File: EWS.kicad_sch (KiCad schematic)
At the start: 4 parts

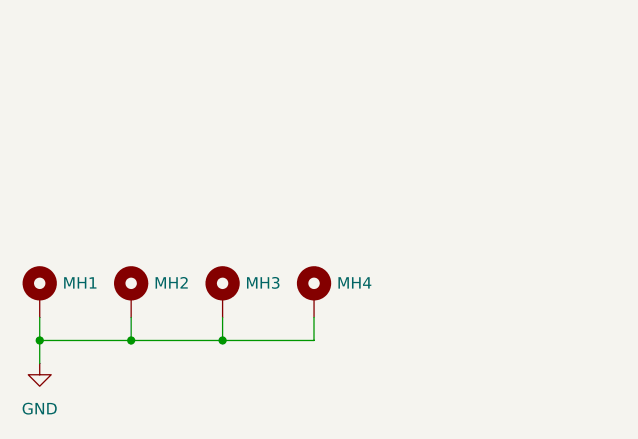
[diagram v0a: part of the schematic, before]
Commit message: Major hardware update: toolhead switching, DC/DC protection, and documentation overhaul
Hardware Changes:
- Replaced reverse polarity protection with 2x PFET toolhead switching (PB2/PA5 control)
- Added SS56 Schottky diode reverse polarity protection for DC/DC converter
- Updated current limit resistor to 5.1kΩ (~10.2A)
- Removed fan control circuitry and JST-XH connector
- Removed internal JST-XH USB port with fuse/protection

Documentation Updates:
- Updated both README files to reflect hardware changes
- Removed all fan control references and configurations
- Updated Klipper configuration examples
- Cleaned up pinout and connector assignments
- Updated technical specifications table
- Fixed table of contents and cross-references
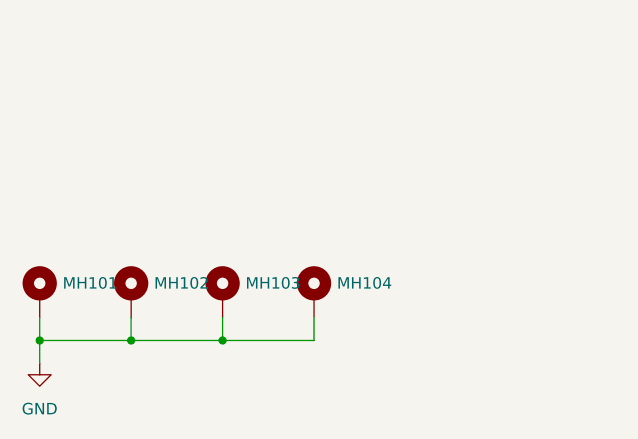
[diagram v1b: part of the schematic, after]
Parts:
- renumbered MH1 to MH101, MH2 to MH102, MH3 to MH103, MH4 to MH104
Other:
- company: (none) -> Eduard Iten
- title: (none) -> EWS - Power, CANbus and USB HAT for 3D Printers
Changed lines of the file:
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@@
 	(generator_version "9.0")
 	(paper "A4")
+	(title_block
+		(title "EWS - Power, CANbus and USB HAT for 3D Printers")
+		(date "2025-12-03")
+		(rev "1.0")
+		(company "Eduard Iten")
+	)
 	(junction
 		(at 54.61 176.53)
@@
 		(on_board yes)
 		(dnp no)
-		(property "Reference" "MH2"
+		(property "Reference" "MH102"
 			(at 46.99 170.18 0)
 			(effects
@@
 			(project "EWS"
 				(path "/4ae99543-64c8-472f-befd-04c32f138656"
-					(reference "MH2")
+					(reference "MH102")
 					(unit 1)
 				)
@@
 		(on_board yes)
 		(dnp no)
-		(property "Reference" "MH3"
+		(property "Reference" "MH103"
 			(at 57.15 170.18 0)
 			(effects
@@
 			(project "EWS"
 				(path "/4ae99543-64c8-472f-befd-04c32f138656"
-					(reference "MH3")
+					(reference "MH103")
 					(unit 1)
 				)
@@
 		(on_board yes)
 		(dnp no)
-		(property "Reference" "MH1"
+		(property "Reference" "MH101"
 			(at 36.83 170.18 0)
 			(effects
@@
 			(project ""
 				(path "/4ae99543-64c8-472f-befd-04c32f138656"
-					(reference "MH1")
+					(reference "MH101")
 					(unit 1)
 				)
@@
 		(on_board yes)
 		(dnp no)
-		(property "Reference" "MH4"
+		(property "Reference" "MH104"
 			(at 67.31 170.18 0)
 			(effects
@@
 			(project "EWS"
 				(path "/4ae99543-64c8-472f-befd-04c32f138656"
-					(reference "MH4")
+					(reference "MH104")
 					(unit 1)
 				)

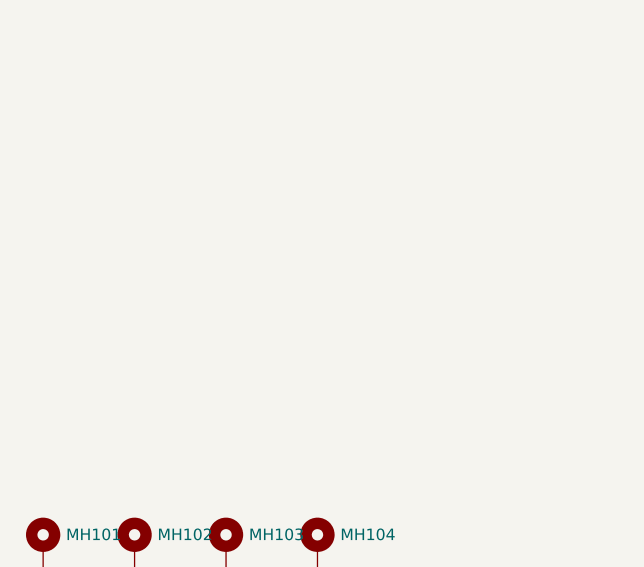
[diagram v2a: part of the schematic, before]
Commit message: Rev 0.2: Major hardware improvements and production readiness
Hardware Improvements (Thanks to shx for schematic cleanup):
- Clean up schematic organization and structure
- Set CAN transceiver Silent pin to GND for stability
- Add status LEDs (yellow: 24V/5V/3.3V, green: MCU PB4)
- Replace jumpers with solder jumpers on bottom side
- Add jumpers to output PFETs for permanent-on without firmware
- Add robust test points for 5V/GND load testing
- Add optional heatsink for DC/DC converter on bottom
- Add 10µF capacitor for MCU on 3.3V rail

Component Optimizations:
- Replace 30kΩ with 33kΩ basic part for simplified BOM
- Change DC/DC feedback: 15.5kΩ15kΩ (new output: 5.1V)
- Upgrade CAN ESD protection: NUP2105LPESD1CAN
- Increase CAN termination resistor footprint: 04020603
- Switch USB hub supply from 5V to 3.3V per datasheet

Production Ready:
- Add all LCSC part numbers and rotations
- Generate complete production data package
- Improve PCB layout and button placement
- Create comprehensive changelog documentation
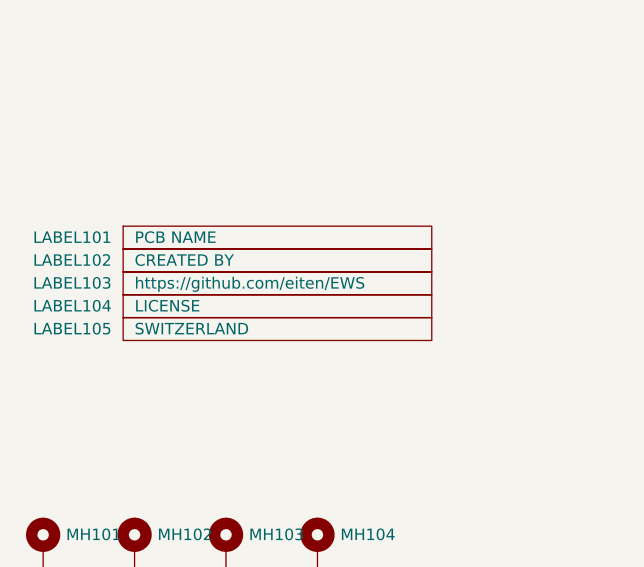
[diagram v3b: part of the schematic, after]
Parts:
- added LABEL101: PCB NAME, project:EWS Rev. 1.0, symbol project:LABEL_PCB_NAME
- added LABEL102: CREATED BY, project:EduardIten, symbol project:LABEL_CREATED_BY
- added LABEL103: https://github.com/eiten/EWS, project:http___github.com_eiten_EWS, symbol project:LABEL_QR_CODE
- added LABEL104: LICENSE, project:CC_BY_NC_SA 4, symbol project:LABEL_LICENSE
- added LABEL105: SWITZERLAND, project:Switzerland, symbol project:LABEL_SWITZERLAND
